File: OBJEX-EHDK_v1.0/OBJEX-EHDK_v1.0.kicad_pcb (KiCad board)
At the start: 2 copper layers, 65 parts, among them J1 Conn_LiPoBattery, J10 Conn_01x02, J11 TestPoint - Black, J12 TestPoint - Red, J13 TestPoint - Purple, J14 TestPoint - Orange, J15 Solar, J16 Vout1, J17 Vout2, J18 Conn_01x02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

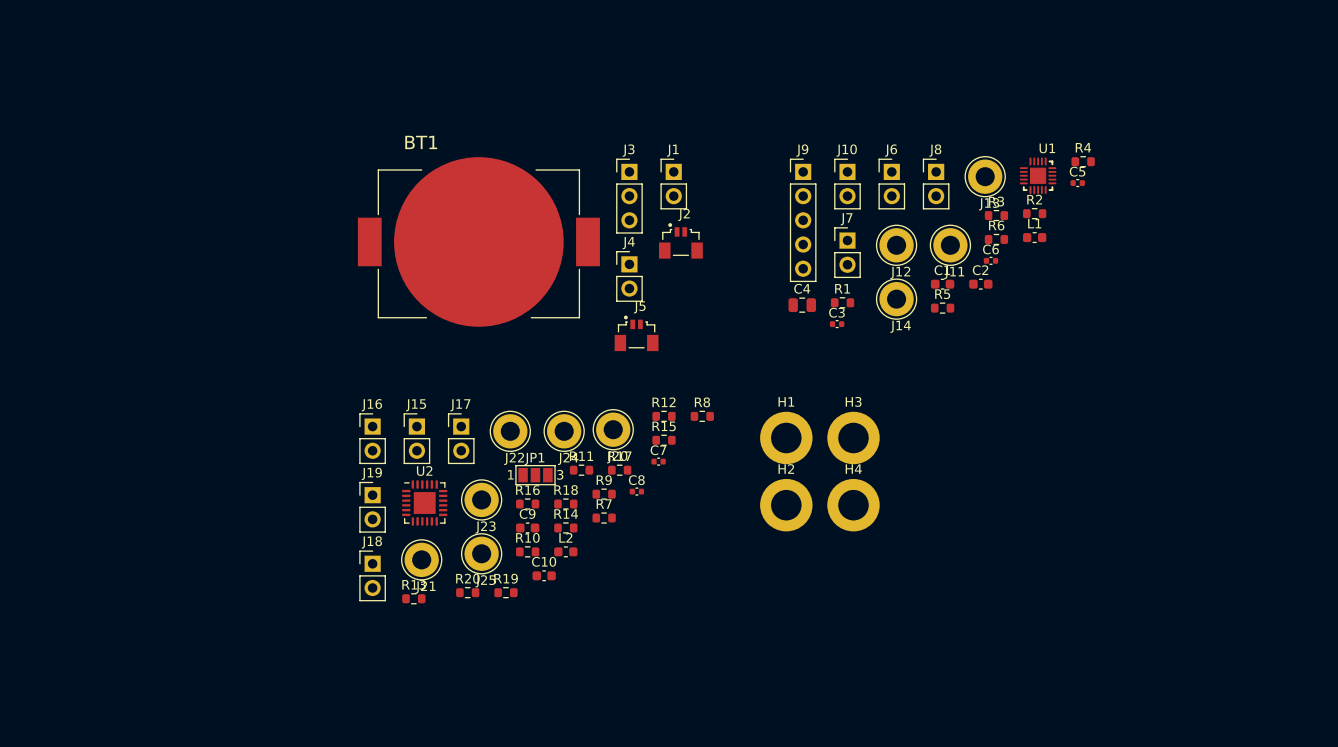
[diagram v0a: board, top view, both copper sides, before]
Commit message: SCH Ready for PCB design
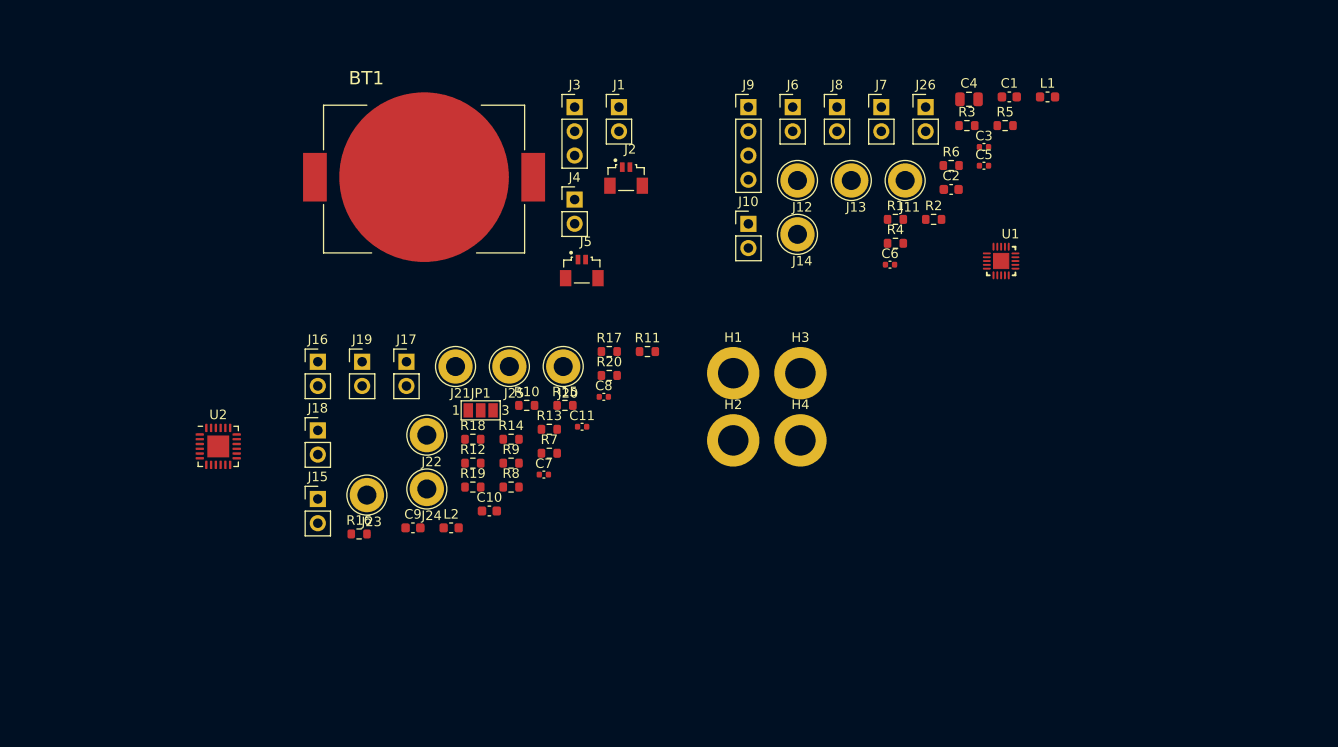
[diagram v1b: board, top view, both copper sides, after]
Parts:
- added C11: 100nF, Capacitor_SMD:C_0402_1005Metric, F.Cu at (110.9, 100.8)
- added J26: Conn_01x02, Connector_PinHeader_2.54mm:PinHeader_1x02_P2.54mm_Vertical, F.Cu at (146.9, 67.3)
- C8: value 10uF -> 10uF/10V
- J9: value Conn_01x05 -> Conn_01x04; footprint Connector_PinHeader_2.54mm:PinHeader_1x05_P2.54mm_Vertical -> Connector_PinHeader_2.54mm:PinHeader_1x04_P2.54mm_Vertical
- moved C4 27.8 mm to (151.5, 66.5)
- moved R20 27.2 mm to (113.7, 95.5)
- moved C3 24.1 mm to (153.1, 71.5)
- moved R13 22.8 mm to (107.4, 101.1)
- moved U2 22.5 mm to (72.7, 102.9)
- moved R4 21.5 mm to (143.8, 81.6)
- moved R8 21.4 mm to (103.4, 107.2)
- moved C1 20.9 mm to (155.7, 66.2)
- moved R12 20.7 mm to (99.4, 104.7)
- moved J21 20.6 mm to (97.6, 94.5)
- moved R5 20.2 mm to (155.3, 69.2)
- moved J25 19.9 mm to (103.2, 94.5)
- moved R16 18.0 mm to (87.5, 112.1)
- moved J24 15.6 mm to (94.6, 107.4)
- moved R10 15.4 mm to (105.1, 98.6)
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
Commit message: SCH first review
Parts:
- added kibuzzard-63010F9B: G***, kibuzzard-63010F9B, F.Cu at (184.3, 83.2)
- added kibuzzard-63010FBF: G***, kibuzzard-63010FBF, F.Cu at (184.2, 80.7)
- moved J16 105.3 mm to (185.7, 117.6), turned to 180 degrees
- moved J17 97.5 mm to (185.7, 122.7)
- moved J15 97.1 mm to (180.2, 109.8), turned to 90 degrees
- moved U2 95.2 mm to (166.8, 117.5)
- moved J23 91.3 mm to (178.5, 122.0)
- moved J22 88.0 mm to (178.6, 128.1)
- moved J21 83.7 mm to (178.4, 116.2)
- moved J24 81.8 mm to (176.3, 104.3)
- moved J18 80.5 mm to (163.5, 106.0)
- moved C9 79.6 mm to (172.7, 115.5), turned to 90 degrees
- moved J25 78.5 mm to (181.1, 104.4)
- moved L2 76.2 mm to (172.7, 121.8), turned to 90 degrees
- moved J19 73.1 mm to (159.9, 106.0)
- moved R14 72.9 mm to (172.7, 125.1), turned to -90 degrees
- moved H1 72.2 mm to (54.5, 95.7)
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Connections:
- H2 pad 1: Net-(H2-Pad1) -> GND
- H4 pad 1: Net-(H2-Pad1) -> GND
- JP1 pad 2: Net-(JP1-Pad2) -> Net-(U2-Pad20)
- R7 pad 1: Net-(JP1-Pad1) -> Net-(JP1-Pad3)
- R8 pad 1: Net-(JP1-Pad2) -> Net-(JP1-Pad1)
- U2 pad 20: Net-(JP1-Pad3) -> Net-(U2-Pad20)

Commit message: PCB design update
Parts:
- removed kibuzzard-63010F9B: G***, kibuzzard-63010F9B
- removed kibuzzard-63010FBF: G***, kibuzzard-63010FBF
- moved H2 99.8 mm to (153.1, 118.4)
- moved H3 97.2 mm to (153.1, 62.9)
- moved J25 68.8 mm to (112.5, 110.0)
- moved J11 66.5 mm to (112.5, 72.0)
- moved J24 57.8 mm to (119.4, 94.5)
- moved H1 51.5 mm to (94.2, 62.8)
- moved J22 51.2 mm to (128.6, 116.8)
- moved J15 40.9 mm to (140.6, 119.8), turned to -90 degrees
- moved C11 38.8 mm to (134.1, 109.4)
- moved J23 36.9 mm to (145.0, 106.7)
- moved C7 36.8 mm to (132.0, 108.7), turned to 180 degrees
- moved J26 36.3 mm to (123.9, 80.9)
- moved J10 36.3 mm to (121.4, 88.1)
- moved J9 36.3 mm to (129.0, 84.5)
- moved J21 36.3 mm to (145.0, 102.0)
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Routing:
- net /BatteryConnectors/BATT_SPV1050: track 0.00 -> 66.3 mm, vias 0 -> 1
- net /ADP5091/BATT_ADP5091: track 0.00 -> 44.1 mm, vias 0 -> 1
- net Net-(BT1-PadP1): track 0.00 -> 40.4 mm
- net /ADP5091/SolarPanel: track 0.00 -> 32.1 mm, vias 0 -> 2
- net /ADP5091/BACKUP-BATT_ADP5091: track 0.00 -> 30.3 mm, vias 0 -> 1
- net /SPV1050TTR/STORE: track 0.00 -> 29.6 mm, vias 0 -> 2
- net /SPV1050TTR/LDO_EN_3V3: track 0.00 -> 20.4 mm
- net /ADP5091/Vout(Sens): track 0.00 -> 20.1 mm
- net /ADP5091/Vout(MCU): track 0.00 -> 19.6 mm
- net /SPV1050TTR/Vout_3V3: track 0.00 -> 18.8 mm
- net /SPV1050TTR/Vout_1V8: track 0.00 -> 18.3 mm
- net /SPV1050TTR/PV_MODULE: track 0.00 -> 15.9 mm
- net Net-(R10-Pad2): track 0.00 -> 15.6 mm
- net Net-(R14-Pad2): track 0.00 -> 15.5 mm, vias 0 -> 2
- net /SPV1050TTR/LDO_EN_1V8: track 0.00 -> 15.1 mm
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- added copper zone on B.Cu, net GND
- added copper zone on F.Cu, net GND
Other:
- board outline added: 65.4 x 62.1 mm

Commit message: update design
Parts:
- added kibuzzard-6307AAC8: G***, kibuzzard-6307AAC8, F.Cu at (145.0, 96.7)
- added kibuzzard-6307AAE6: G***, kibuzzard-6307AAE6, F.Cu at (145.0, 112.0)
- added kibuzzard-6307AB03: G***, kibuzzard-6307AB03, F.Cu at (145.0, 81.3)
- added kibuzzard-6307AB19: G***, kibuzzard-6307AB19, F.Cu at (145.0, 68.3)
- added kibuzzard-6307AB8B: G***, kibuzzard-6307AB8B, F.Cu at (117.4, 64.0)
- added kibuzzard-6307AB8B: G***, kibuzzard-6307AB8B, F.Cu at (152.2, 79.8)
- added kibuzzard-6307AB8B: G***, kibuzzard-6307AB8B, F.Cu at (152.2, 69.9)
- added kibuzzard-6307AB8B: G***, kibuzzard-6307AB8B, F.Cu at (152.2, 99.4)
- added kibuzzard-6307AB8B: G***, kibuzzard-6307AB8B, F.Cu at (140.6, 117.4)
- added kibuzzard-6307AB8B: G***, kibuzzard-6307AB8B, F.Cu at (152.2, 109.2)
- added kibuzzard-6307AB8B: G***, kibuzzard-6307AB8B, F.Cu at (117.4, 117.1)
- added kibuzzard-6307AB8B: G***, kibuzzard-6307AB8B, F.Cu at (125.5, 93.5)
- added kibuzzard-6307AB8B: G***, kibuzzard-6307AB8B, F.Cu at (125.4, 100.8)
- added kibuzzard-6307AB8B: G***, kibuzzard-6307AB8B, F.Cu at (140.6, 63.9)
- added kibuzzard-6307AD03: G***, kibuzzard-6307AD03, F.Cu at (129.0, 100.8)
- added kibuzzard-6307AD08: G***, kibuzzard-6307AD08, F.Cu at (129.1, 93.5)
- added kibuzzard-6307AD98: G***, kibuzzard-6307AD98, F.Cu at (133.5, 113.9)
- added kibuzzard-6307ADF4: G***, kibuzzard-6307ADF4, F.Cu at (122.7, 78.3)
- added kibuzzard-6307B472: G***, kibuzzard-6307B472, F.Cu at (103.8, 63.2)
- added kibuzzard-6307B472: G***, kibuzzard-6307B472, F.Cu at (114.3, 83.9)
- added kibuzzard-6307B497: G***, kibuzzard-6307B497, F.Cu at (114.3, 98.1)
- added kibuzzard-6307B497: G***, kibuzzard-6307B497, F.Cu at (103.9, 118.2)
- added kibuzzard-6307B557: G***, kibuzzard-6307B557, F.Cu at (119.7, 91.0)
- added kibuzzard-6307B6B8: G***, kibuzzard-6307B6B8, F.Cu at (114.8, 64.0)
- added kibuzzard-6307B6B8: G***, kibuzzard-6307B6B8, F.Cu at (114.8, 117.1)
- added kibuzzard-6307B74A: G***, kibuzzard-6307B74A, F.Cu at (104.0, 120.0)
- added kibuzzard-6307B77B: G***, kibuzzard-6307B77B, F.Cu at (104.0, 61.3)
- moved J24 3.50 mm to (119.4, 98.0)
- moved J18 0.95 mm to (129.0, 95.9)
- moved J19 0.95 mm to (125.4, 95.9)
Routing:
- net /ADP5091/BACKUP-BATT_ADP5091: track 30.3 -> 31.7 mm
- net /ADP5091/REG_D0: track 7.47 -> 6.36 mm
- net /ADP5091/REG_D1: track 10.1 -> 9.20 mm

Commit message: update
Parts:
- added G***: LOGO, KicadLibrary:logov2-big, F.Cu at (100.4, 108.7)
- added kibuzzard-630A2C1A: G***, kibuzzard-630A2C1A, F.Cu at (137.9, 63.9)
- added kibuzzard-630A2C1A: G***, kibuzzard-630A2C1A, F.Cu at (138.0, 117.4)
- added kibuzzard-630A2CD4: G***, kibuzzard-630A2CD4, F.Cu at (99.4, 111.2)
- moved kibuzzard-6307AD98 5.00 mm to (128.5, 113.9)
- moved J22 4.90 mm to (133.5, 116.7)
- moved J20 4.90 mm to (128.5, 116.8)
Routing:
- net /ADP5091/SolarPanel: track 32.1 -> 27.0 mm
- net /ADP5091/LLD: track 11.7 -> 15.7 mm

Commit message: last review
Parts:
- removed kibuzzard-6307AAE6: G***, kibuzzard-6307AAE6
- removed kibuzzard-6307ADF4: G***, kibuzzard-6307ADF4
- added J27: TestPoint - Purple, TestPoint:TestPoint_Loop_D3.80mm_Drill2.0mm, F.Cu at (123.4, 116.8)
- added kibuzzard-6307AB8B: G***, kibuzzard-6307AB8B, F.Cu at (123.4, 113.9)
- added kibuzzard-630DCDF3: G***, kibuzzard-630DCDF3, F.Cu at (145.0, 112.4)
- added kibuzzard-630DD246: G***, kibuzzard-630DD246, F.Cu at (124.0, 74.8)
- added kibuzzard-630DD25A: G***, kibuzzard-630DD25A, F.Cu at (121.5, 74.8)
- added kibuzzard-630DD299: G***, kibuzzard-630DD299, F.Cu at (126.5, 80.0)
- added kibuzzard-630DD2B3: G***, kibuzzard-630DD2B3, F.Cu at (129.0, 80.4)
- added kibuzzard-630DD2DE: G***, kibuzzard-630DD2DE, F.Cu at (128.5, 88.1)
- added kibuzzard-630DD324: G***, kibuzzard-630DD324, F.Cu at (151.7, 89.4)
- added kibuzzard-630DD339: G***, kibuzzard-630DD339, F.Cu at (151.7, 92.6)
